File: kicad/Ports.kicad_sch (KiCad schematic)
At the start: 6 parts, among them J1 SWD, J2 CAN, J3 Conn_01x01_Socket, J4 Conn_01x01_Socket, J5 Conn_01x01_Socket, J6 Conn_01x01_Socket

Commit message: Placed status LEDs
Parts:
- removed J1: SWD, symbol Connector:Conn_01x04_Male
- added J1: SWD, symbol Connector:Conn_01x05_Pin
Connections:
- new net +3.3V: J1.1 (Pin_1)
- new net GND: J1.3 (Pin_3)
- new net NRST: J1.5 (Pin_5)
- new net SWDCLK: J1.2 (Pin_2)
- new net SWDIO: J1.4 (Pin_4)
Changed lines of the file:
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@@
+    )
+  )
+  (global_label "SWDCLK" (shape output) (at 73.66 34.29 0) (fields_autoplaced)
+    (effects (font (size 1.27 1.27)) (justify left))
+    (property "Intersheetrefs" "${INTERSHEET_REFS}" (at 84.1442 34.29 0)
+      (effects (font (size 1.27 1.27)) (justify left) hide)
     )
   )
@@
     )
   )
+  (global_label "NRST" (shape output) (at 73.66 41.91 0) (fields_autoplaced)
+    (effects (font (size 1.27 1.27)) (justify left))
+    (property "Intersheetrefs" "${INTERSHEET_REFS}" (at 81.4228 41.91 0)
+      (effects (font (size 1.27 1.27)) (justify left) hide)
+    )
+  )
+  (global_label "SWDIO" (shape bidirectional) (at 73.66 39.37 0) (fields_autoplaced)
+    (effects (font (size 1.27 1.27)) (justify left))
+    (property "Intersheetrefs" "${INTERSHEET_REFS}" (at 83.6227 39.37 0)
+      (effects (font (size 1.27 1.27)) (justify left) hide)
+    )
+  )
   (symbol (lib_id "Connector:Conn_01x01_Socket") (at 38.1 38.1 180) (unit 1)
     (in_bom yes) (on_board yes) (dnp no) (fields_autoplaced)
@@
     )
   )
-  (symbol (lib_id "Connector:Conn_01x01_Socket") (at 38.1 43.18 180) (unit 1)
-    (in_bom yes) (on_board yes) (dnp no) (fields_autoplaced)
-    (property "Reference" "J6" (at 38.735 40.64 0)
-      (effects (font (size 1.27 1.27)))
-    )
-    (property "Value" "Conn_01x01_Socket" (at 38.735 40.64 0)
-      (effects (font (size 1.27 1.27)) hide)
-    )
-    (property "Footprint" "" (at 38.1 43.18 0)
-      (effects (font (size 1.27 1.27)) hide)
-    )
-    (property "Datasheet" "~" (at 38.1 43.18 0)
-      (effects (font (size 1.27 1.27)) hide)
-    )
-    (pin "1")
-    (instances
-      (project "sBMS"
-        (path "/7f25f26f-13d1-483f-a85d-b3abae309e30"
-          (reference "J6") (unit 1)
-        )
-        (path "/7f25f26f-13d1-483f-a85d-b3abae309e30/3045692e-7230-49c2-a7e4-9d00ed8073c1"
-          (reference "J6") (unit 1)
-        )
-      )
-    )
-  )
-  (symbol (lib_id "Connector:Conn_01x04_Male") (at 73.66 36.83 0) (unit 1)
-    (in_bom yes) (on_board yes) (dnp no)
-    (property "Reference" "J1" (at 76.2 29.21 0)
-      (effects (font (size 1.27 1.27)))
-    )
-    (property "Value" "SWD" (at 76.2 31.75 0)
-      (effects (font (size 1.27 1.27)))
-    )
-    (property "Footprint" "" (at 73.66 36.83 0)
-      (effects (font (size 1.27 1.27)) hide)
-    )
-    (property "Datasheet" "~" (at 73.66 36.83 0)
+  (symbol (lib_id "Connector:Conn_01x05_Pin") (at 68.58 36.83 0) (unit 1)
+    (in_bom yes) (on_board yes) (dnp no) (fields_autoplaced)
+    (property "Reference" "J1" (at 69.215 26.67 0)
+      (effects (font (size 1.27 1.27)))
+    )
+    (property "Value" "SWD" (at 69.215 29.21 0)
+      (effects (font (size 1.27 1.27)))
+    )
+    (property "Footprint" "" (at 68.58 36.83 0)
+      (effects (font (size 1.27 1.27)) hide)
+    )
+    (property "Datasheet" "~" (at 68.58 36.83 0)
       (effects (font (size 1.27 1.27)) hide)
     )
@@
     (pin "3")
     (pin "4")
-    (instances
-      (project "sBMS"
-        (path "/7f25f26f-13d1-483f-a85d-b3abae309e30"
+    (pin "5")
+    (instances
+      (project "sBMS"
+        (path "/7f25f26f-13d1-483f-a85d-b3abae309e30/3045692e-7230-49c2-a7e4-9d00ed8073c1"
           (reference "J1") (unit 1)
         )
-        (path "/7f25f26f-13d1-483f-a85d-b3abae309e30/3045692e-7230-49c2-a7e4-9d00ed8073c1"
-          (reference "J1") (unit 1)
+      )
+    )
+  )
+  (symbol (lib_id "power:+3.3V") (at 73.66 31.75 270) (unit 1)
+    (in_bom yes) (on_board yes) (dnp no) (fields_autoplaced)
+    (property "Reference" "#PWR02" (at 69.85 31.75 0)
+      (effects (font (size 1.27 1.27)) hide)
+    )
+    (property "Value" "+3.3V" (at 77.47 31.75 90)
+      (effects (font (size 1.27 1.27)) (justify left))
+    )
+    (property "Footprint" "" (at 73.66 31.75 0)
+      (effects (font (size 1.27 1.27)) hide)
+    )
+    (property "Datasheet" "" (at 73.66 31.75 0)
+      (effects (font (size 1.27 1.27)) hide)
+    )
+    (pin "1")
+    (instances
+      (project "sBMS"
+        (path "/7f25f26f-13d1-483f-a85d-b3abae309e30/3045692e-7230-49c2-a7e4-9d00ed8073c1"
+          (reference "#PWR02") (unit 1)
+        )
+      )
+    )
+  )
+  (symbol (lib_id "Connector:Conn_01x01_Socket") (at 38.1 43.18 180) (unit 1)
+    (in_bom yes) (on_board yes) (dnp no) (fields_autoplaced)
+    (property "Reference" "J6" (at 38.735 40.64 0)
+      (effects (font (size 1.27 1.27)))
+    )
+    (property "Value" "Conn_01x01_Socket" (at 38.735 40.64 0)
+      (effects (font (size 1.27 1.27)) hide)
+    )
+    (property "Footprint" "" (at 38.1 43.18 0)
+      (effects (font (size 1.27 1.27)) hide)
+    )
+    (property "Datasheet" "~" (at 38.1 43.18 0)
+      (effects (font (size 1.27 1.27)) hide)
+    )
+    (pin "1")
+    (instances
+      (project "sBMS"
+        (path "/7f25f26f-13d1-483f-a85d-b3abae309e30"
+          (reference "J6") (unit 1)
+        )
+        (path "/7f25f26f-13d1-483f-a85d-b3abae309e30/3045692e-7230-49c2-a7e4-9d00ed8073c1"
+          (reference "J6") (unit 1)
         )
       )
@@
         )
       )
+    )
+  )
+  (symbol (lib_id "power:GND") (at 73.66 36.83 90) (unit 1)
+    (in_bom yes) (on_board yes) (dnp no) (fields_autoplaced)
+    (property "Reference" "#PWR024" (at 80.01 36.83 0)
+      (effects (font (size 1.27 1.27)) hide)
+    )
+    (property "Value" "GND" (at 77.47 36.83 90)
+      (effects (font (size 1.27 1.27)) (justify right))
+    )
+    (property "Footprint" "" (at 73.66 36.83 0)
+      (effects (font (size 1.27 1.27)) hide)
+    )
+    (property "Datasheet" "" (at 73.66 36.83 0)
+      (effects (font (size 1.27 1.27)) hide)
+    )
+    (pin "1")
+    (instances
+      (project "sBMS"
+        (path "/7f25f26f-13d1-483f-a85d-b3abae309e30/3045692e-7230-49c2-a7e4-9d00ed8073c1"
+          (reference "#PWR024") (unit 1)
+        )
+      )

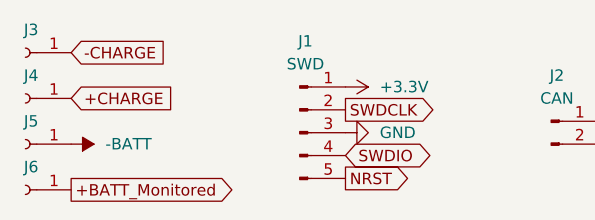
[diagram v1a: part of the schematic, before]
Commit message: Added charge MOSFET
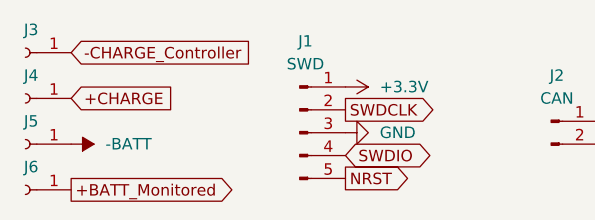
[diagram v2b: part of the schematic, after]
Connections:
- net -CHARGE renamed -CHARGE_Controller
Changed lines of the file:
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@@
   (title_block
     (title "Ports/Connectors")
-    (date "2023-08-20")
+    (date "2023-09-06")
     (rev "1")
     (company "Dynamium")
@@
     )
   )
-  (global_label "-CHARGE" (shape input) (at 43.18 27.94 0) (fields_autoplaced)
+  (global_label "-CHARGE_Controller" (shape input) (at 43.18 27.94 0) (fields_autoplaced)
     (effects (font (size 1.27 1.27)) (justify left))
-    (property "Intersheetrefs" "${INTERSHEET_REFS}" (at 55.1157 27.94 0)
+    (property "Intersheetrefs" "${INTERSHEET_REFS}" (at 65.5174 27.94 0)
       (effects (font (size 1.27 1.27)) (justify left) hide)
     )

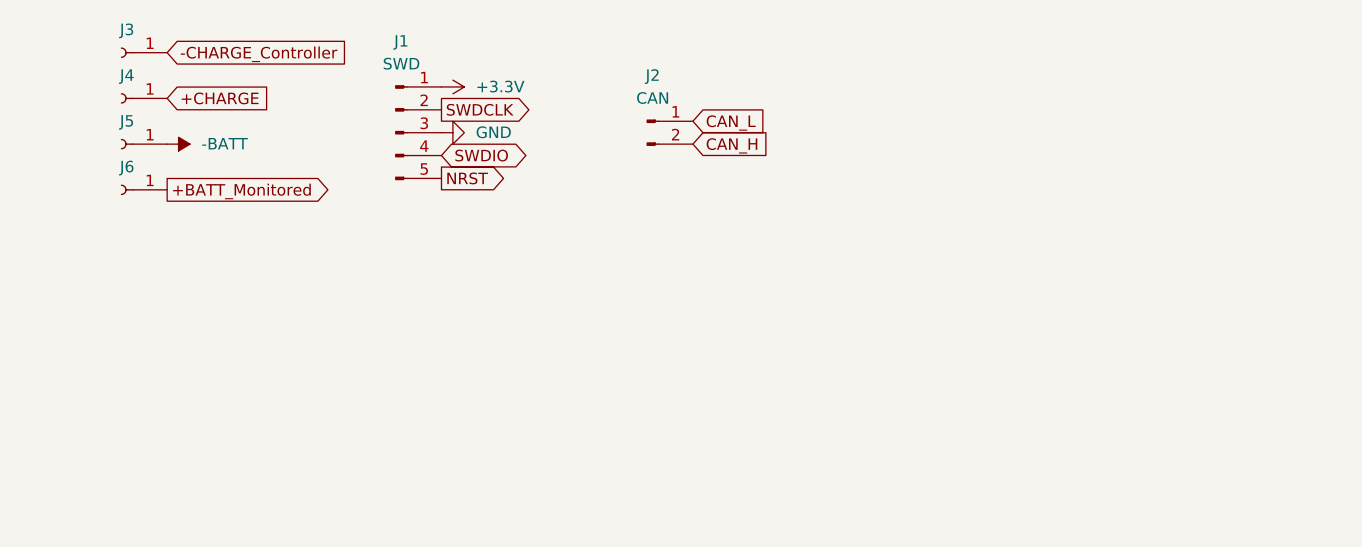
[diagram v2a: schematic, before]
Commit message: fixed typo in ports
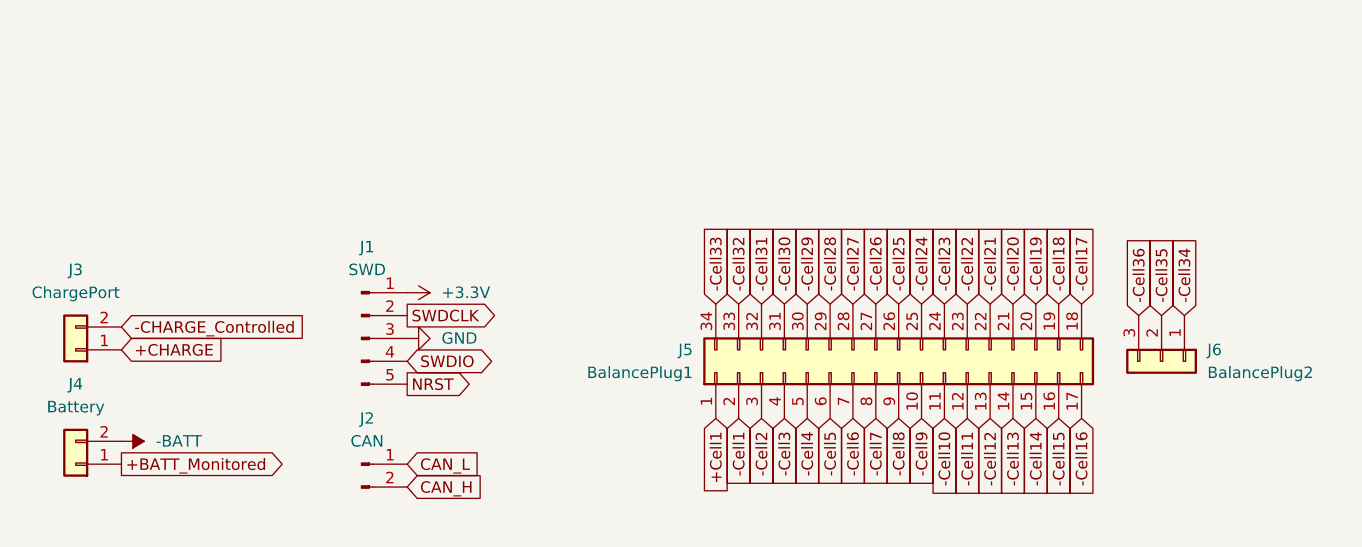
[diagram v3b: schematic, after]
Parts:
- removed J3, J4, J5, J6: Conn_01x01_Socket, symbol Connector:Conn_01x01_Socket
- added J3: ChargePort, symbol Connector_Generic:Conn_01x02
- added J4: Battery, symbol Connector_Generic:Conn_01x02
- added J5: BalancePlug1, Connector_JST:JST_PHD_S34B-PHDSS_2x17_P2.00mm_Horizontal, symbol Connector_Generic:Conn_02x17_Counter_Clockwise
- added J6: BalancePlug2, Connector_JST:JST_PH_S3B-PH-K_1x03_P2.00mm_Horizontal, symbol Connector_Generic:Conn_01x03
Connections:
- net +BATT_Monitored: now also J4.1 (Pin_1)
- net +CHARGE: now also J3.1 (Pin_1)
- net -BATT: now also J4.2 (Pin_2)
- new net +Cell1: J5.1 (Pin_1)
- new net -CHARGE_Controlled: J3.2 (Pin_2)
- new net -Cell1: J5.2 (Pin_2)
- new net -Cell10: J5.11 (Pin_11)
- new net -Cell11: J5.12 (Pin_12)
- new net -Cell12: J5.13 (Pin_13)
- new net -Cell13: J5.14 (Pin_14)
- new net -Cell14: J5.15 (Pin_15)
- new net -Cell15: J5.16 (Pin_16)
- new net -Cell16: J5.17 (Pin_17)
- new net -Cell17: J5.18 (Pin_18)
- new net -Cell18: J5.19 (Pin_19)
- new net -Cell19: J5.20 (Pin_20)
- new net -Cell2: J5.3 (Pin_3)
- new net -Cell20: J5.21 (Pin_21)
- new net -Cell21: J5.22 (Pin_22)
- new net -Cell22: J5.23 (Pin_23)
- new net -Cell23: J5.24 (Pin_24)
- new net -Cell24: J5.25 (Pin_25)
- new net -Cell25: J5.26 (Pin_26)
- new net -Cell26: J5.27 (Pin_27)
- new net -Cell27: J5.28 (Pin_28)
- new net -Cell28: J5.29 (Pin_29)
- new net -Cell29: J5.30 (Pin_30)
- new net -Cell3: J5.4 (Pin_4)
- new net -Cell30: J5.31 (Pin_31)
- new net -Cell31: J5.32 (Pin_32)
- new net -Cell32: J5.33 (Pin_33)
- new net -Cell33: J5.34 (Pin_34)
- new net -Cell34: J6.1 (Pin_1)
- new net -Cell35: J6.2 (Pin_2)
- new net -Cell36: J6.3 (Pin_3)
- new net -Cell4: J5.5 (Pin_5)
- new net -Cell5: J5.6 (Pin_6)
- new net -Cell6: J5.7 (Pin_7)
- new net -Cell7: J5.8 (Pin_8)
- new net -Cell8: J5.9 (Pin_9)
- new net -Cell9: J5.10 (Pin_10)
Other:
- moved on the sheet: J1, J2
